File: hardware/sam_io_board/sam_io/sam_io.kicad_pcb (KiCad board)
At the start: 2 copper layers, 100 x 100 mm, 162 parts, among them J1 Conn_01x06, J13 J13 DEDICATED D17-D24, J2 J2 DEDICATED D1-D8, J20 nmount SW Debug, J3 J3 DEDICATED D9-D16, J4 USB_C_Receptacle_USB2.0, J5 Conn_01x06, J9 SAM BUS, Q1 2N7002, SW1 Reset, SW2 Boot, SW3 ADDRESS, U1 ADM3483, U3 RP2354B, U4 LMV321, U5 SN74AHCT1G125, U6 AP2112K-3.3, U7 SN74LVC8T245, U8 74AHCT541, Y1 12MHz,18pF

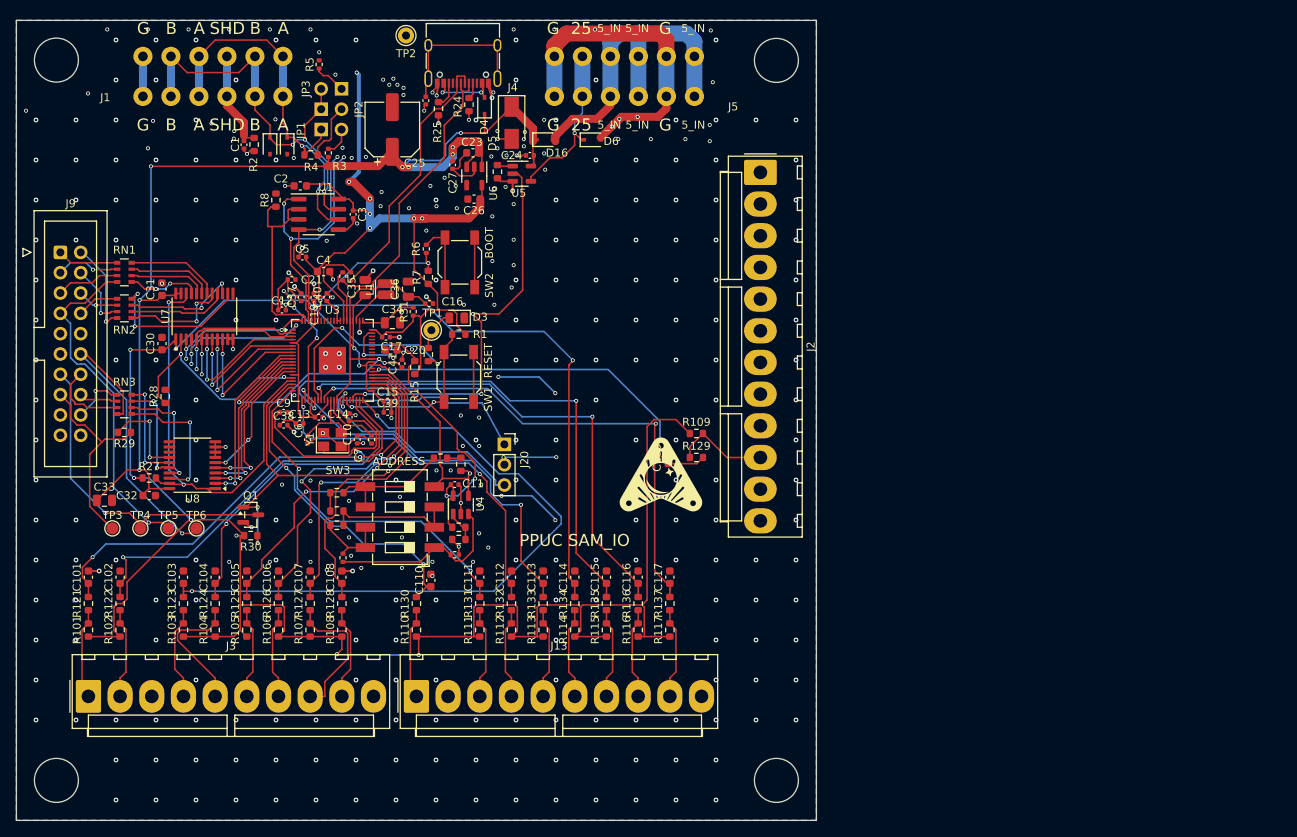
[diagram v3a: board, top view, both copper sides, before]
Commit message: SAM_IO rev 0.2: rotate board, put J13/J3/J2 on the original CPU board harness spots
Board rotated 90 degrees clockwise (J9 top, J1/J5 right) and widened to
158 x 100 mm. J13 (left edge), J3 and J2 (bottom edge) sit at the pin
positions of the original 520-5246-00 CPU board, with the board's
bottom-left corner on the CPU board's bottom-left corner. KK-396 friction
ramps face the board inside. Connector nets rerouted; DRC 0 unconnected.

Co-Authored-By: Claude Opus 5.5 (1M context) <noreply@anthropic.com>
Claude-Session: https://claude.ai/code/session_01Mh8jyzQSZ4SYbwGJXqcn3P
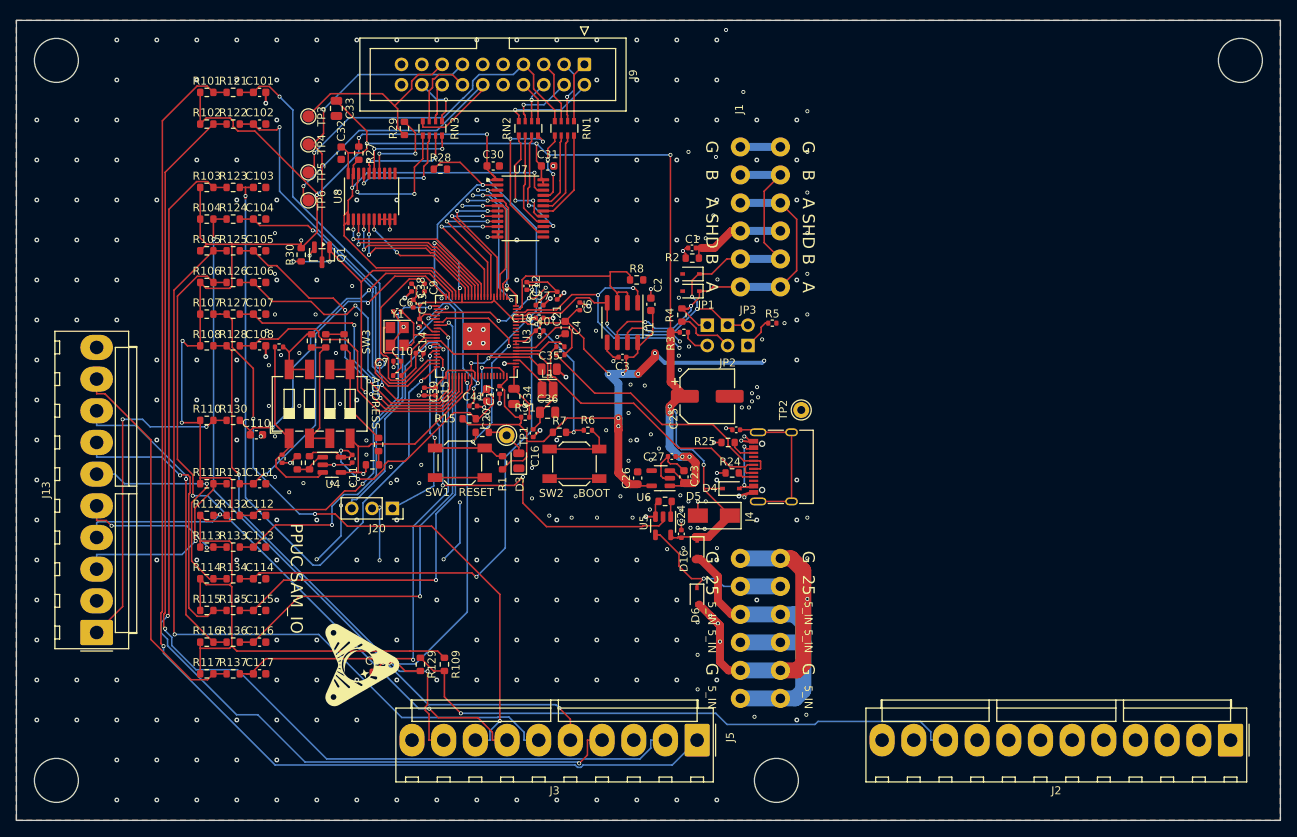
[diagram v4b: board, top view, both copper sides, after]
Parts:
- moved REF** 148.0 mm to (228.0, 44.0), turned to -90 degrees
- moved J2 92.1 mm to (226.8, 129.0), turned to 180 degrees
- moved REF** 90.0 mm to (80.0, 44.0), turned to -90 degrees
- moved REF** 90.0 mm to (80.0, 134.0), turned to -90 degrees
- moved REF** 90.0 mm to (170.0, 134.0), turned to -90 degrees
- moved J5 81.0 mm to (170.5, 123.8), turned to 90 degrees
- moved J3 76.3 mm to (160.1, 129.0), turned to 180 degrees
- moved J9 69.6 mm to (146.0, 44.5), turned to -90 degrees
- moved R101 68.8 mm to (98.8, 48.0), turned to 0 degrees
- moved J1 68.5 mm to (170.5, 72.3), turned to 90 degrees
- moved TP2 68.1 mm to (173.1, 87.7), turned to -90 degrees
- moved R121 66.4 mm to (102.1, 48.0), turned to 0 degrees
- moved J4 65.3 mm to (170.8, 94.8), turned to 90 degrees
- moved R5 65.2 mm to (169.5, 76.8), turned to 0 degrees
- moved C101 64.3 mm to (105.4, 48.0), turned to 0 degrees
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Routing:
- net /Dedicated switches/IN_D9: track 11.4 -> 150.9 mm, vias 0 -> 1
- net /Dedicated switches/IN_D10: track 11.4 -> 139.0 mm, vias 0 -> 1
- net /Dedicated switches/IN_D11: track 11.7 -> 127.0 mm, vias 0 -> 2
- net /Dedicated switches/IN_D13: track 11.4 -> 103.3 mm, vias 0 -> 1
- net /Dedicated switches/IN_D12: track 16.7 -> 94.6 mm, vias 0 -> 2
- net /Dedicated switches/IN_D14: track 11.4 -> 85.9 mm, vias 0 -> 2
- net /Dedicated switches/IN_D15: track 17.7 -> 80.2 mm, vias 0 -> 3
- net /Dedicated switches/IN_MEMPROT: track 12.1 -> 72.7 mm, vias 0 -> 1
- net /Dedicated switches/IN_D16: track 11.7 -> 65.5 mm, vias 0 -> 2
- net /Dedicated switches/IN_D24: track 11.4 -> 47.8 mm
- net /Dedicated switches/IN_D17: track 11.4 -> 41.7 mm, vias 0 -> 2
- net /Dedicated switches/IN_D23: track 11.4 -> 39.5 mm, vias 0 -> 1
- net /Dedicated switches/IN_D22: track 11.4 -> 36.5 mm, vias 0 -> 1
- net /Dedicated switches/IN_D21: track 11.4 -> 30.0 mm, vias 0 -> 1
- net /Dedicated switches/IN_D18: track 11.4 -> 24.7 mm, vias 0 -> 1
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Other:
- board size 100 x 100 mm -> 158 x 100 mm

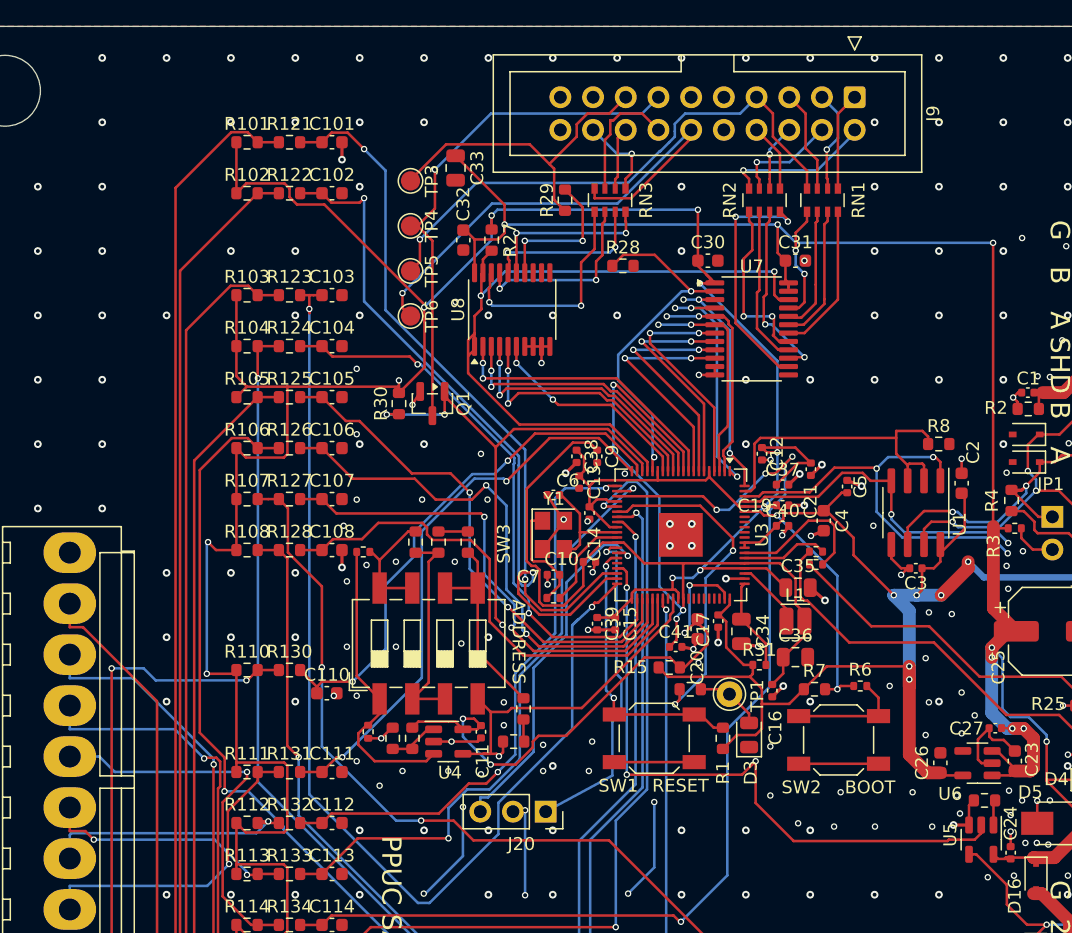
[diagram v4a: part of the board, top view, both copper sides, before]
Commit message: SAM_IO rev 0.2: move J9 to the left edge, turned like the CPU board's J9
J9 now stands vertical on the left edge above J13 on both boards: pin 1 at
the bottom, odd pins and the key notch toward the board centre, as on the
SAM CPU board, so the IO board ribbon arrives from the same side. Bus nets
rerouted with Freerouting (other tracks locked); on the 100 mm board the
logo moved to the old J9 spot, one GND stitch via added and two isolated
stitch vias removed. DRC 0 unconnected on both boards.

Co-Authored-By: Claude Opus 5.5 (1M context) <noreply@anthropic.com>
Claude-Session: https://claude.ai/code/session_01Mh8jyzQSZ4SYbwGJXqcn3P
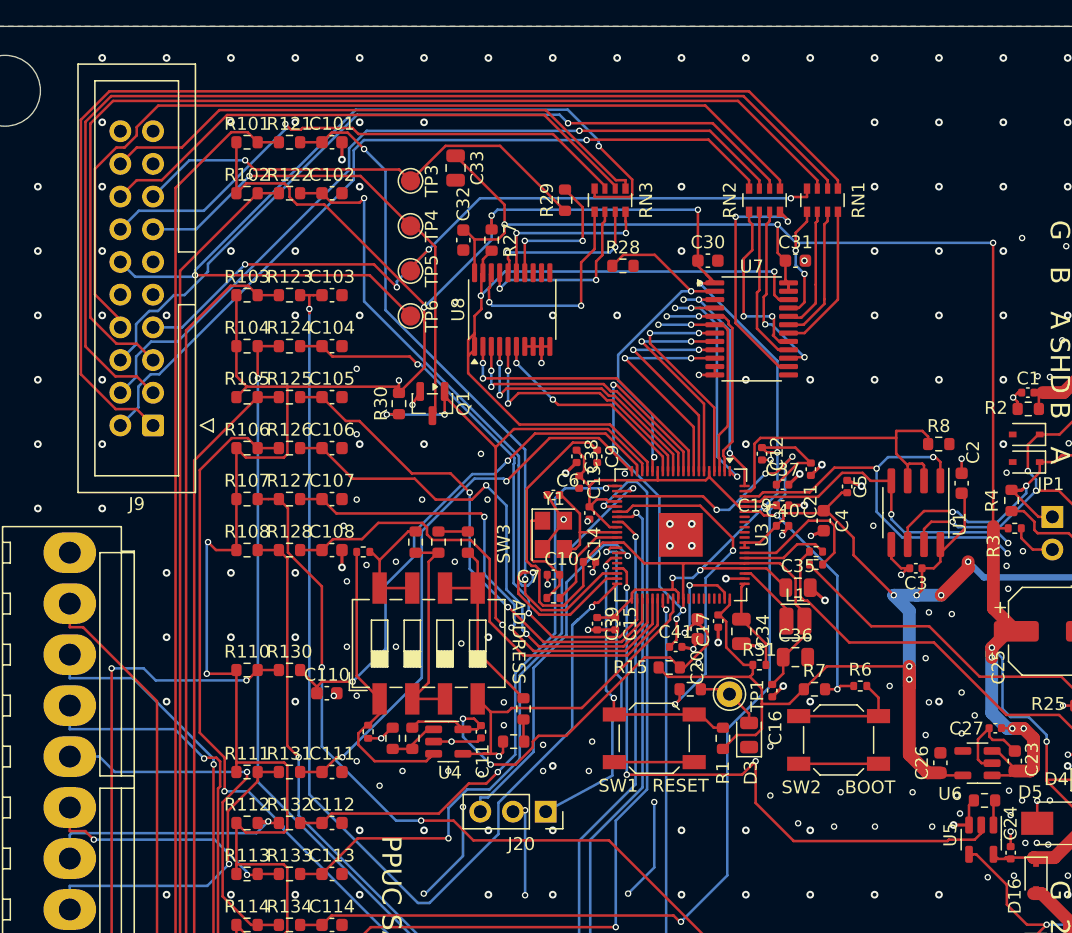
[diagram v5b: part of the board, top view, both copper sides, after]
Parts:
- moved J9 60.2 mm to (91.5, 70.0), turned to 180 degrees
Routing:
- net Net-(J9-Pin_1): track 7.64 -> 90.3 mm
- net Net-(J9-Pin_3): track 8.00 -> 86.0 mm, vias 1 -> 0
- net Net-(J9-Pin_5): track 8.00 -> 81.7 mm
- net Net-(J9-Pin_8): track 5.31 -> 71.8 mm
- net Net-(J9-Pin_6): track 5.19 -> 62.4 mm
- net Net-(J9-Pin_4): track 8.23 -> 62.2 mm
- net Net-(J9-Pin_2): track 11.7 -> 62.3 mm
- net Net-(J9-Pin_16): track 4.90 -> 43.6 mm
- net Net-(J9-Pin_18): track 6.68 -> 43.9 mm, vias 1 -> 0
- net Net-(J9-Pin_14): track 9.97 -> 43.6 mm, vias 0 -> 1
- net Net-(J9-Pin_12): track 40.5 -> 71.2 mm, vias 1 -> 2
- net Net-(J9-Pin_7): track 42.8 -> 59.6 mm, vias 1 -> 4
- net Net-(J9-Pin_15): track 25.4 -> 37.0 mm, vias 0 -> 1
- net Net-(J9-Pin_13): track 40.4 -> 39.1 mm
